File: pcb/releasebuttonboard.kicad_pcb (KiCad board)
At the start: 4 copper layers, 65 x 56 mm, 30 parts, among them SW1 ROTENC, U1 24C16, U2 RASPIPLUSHEADER, U3 OLEDHeader, U4 REncHeader, U5 BtnHeader, U6 PAM8407, U7 REncHeader

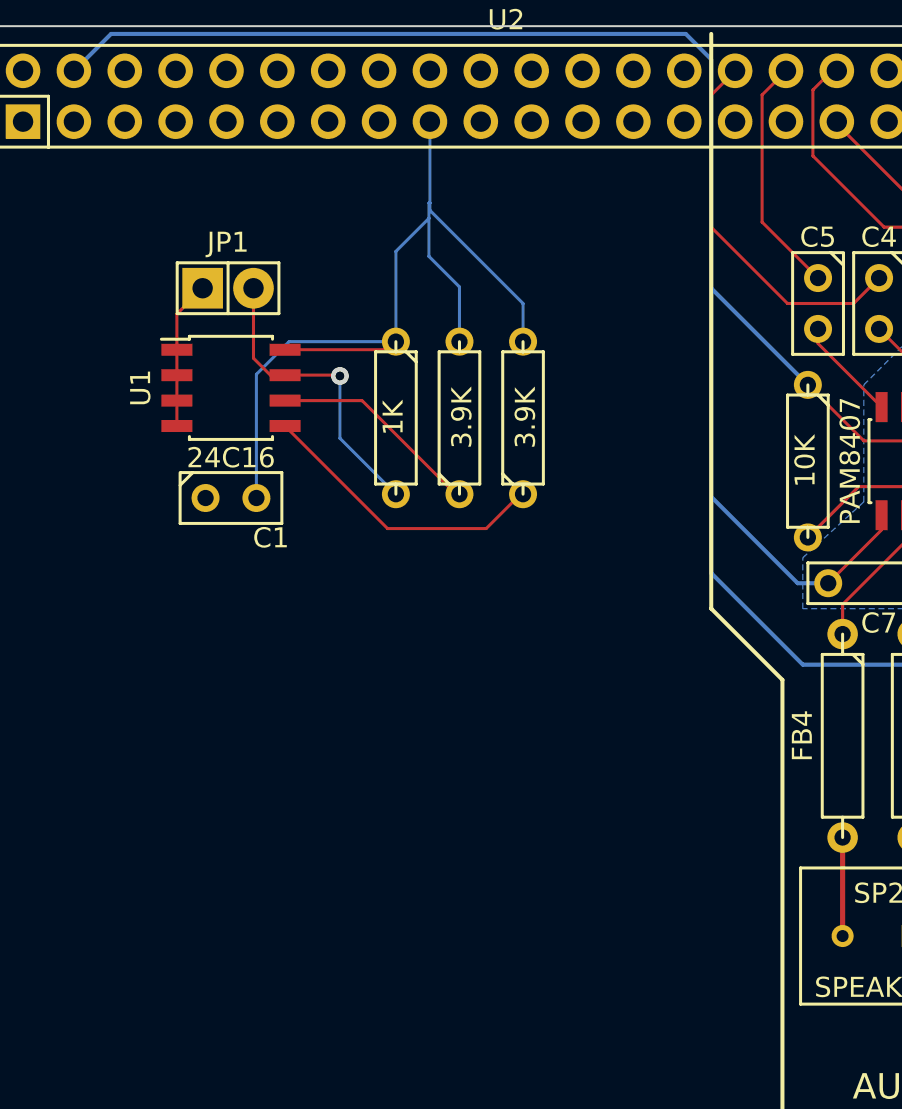
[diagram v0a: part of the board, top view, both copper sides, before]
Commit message: Component placement for ID EEPROM region.
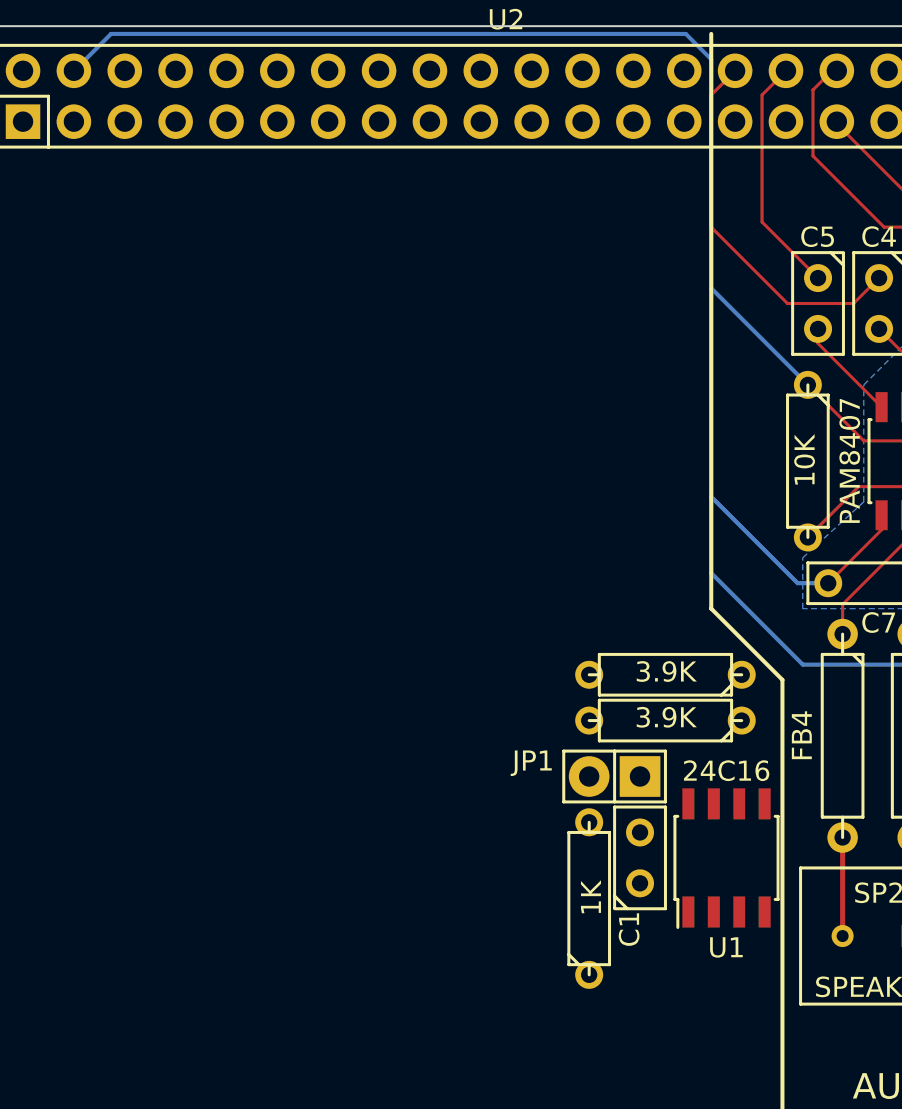
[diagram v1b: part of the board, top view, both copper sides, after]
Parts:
- moved U1 34.1 mm to (139.0, 109.5), turned to 90 degrees
- moved JP1 31.1 mm to (133.4, 105.5), turned to 180 degrees
- moved C1 27.2 mm to (134.7, 109.5), turned to 90 degrees
- moved R1 25.9 mm to (132.1, 111.6), turned to 90 degrees
- moved R3 18.3 mm to (136.0, 102.7), turned to 180 degrees
- moved R2 14.7 mm to (136.0, 100.4), turned to 180 degrees
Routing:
- net VCC: track 69.1 -> 22.3 mm
- net Net-(JP1-Pad2): track 15.2 -> 0.00 mm, vias 1 -> 0
- net /ID_SD: track 14.7 -> 0.00 mm
- net /ID_SC: track 10.8 -> 0.01 mm
- net GND: track 112.9 -> 105.5 mm

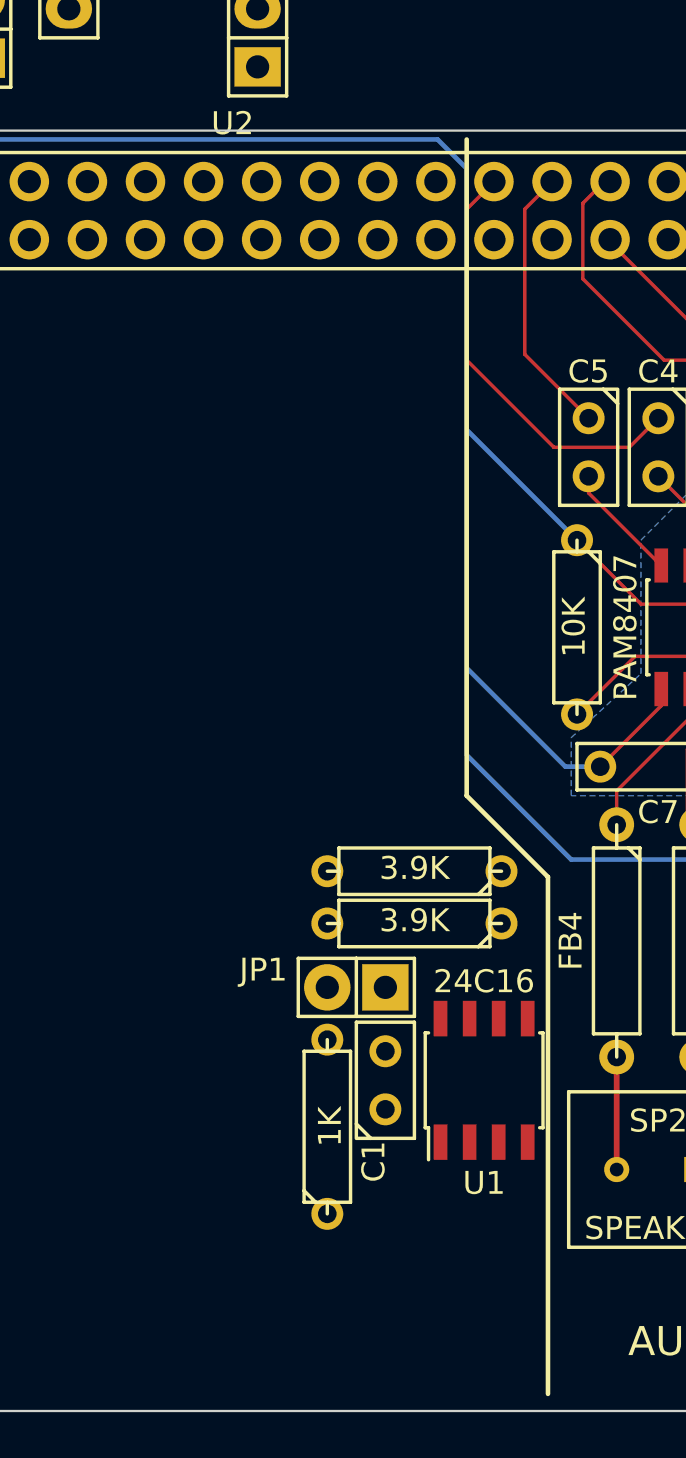
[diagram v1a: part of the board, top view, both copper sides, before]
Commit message: Traces for ID EEPROM circuit portion.
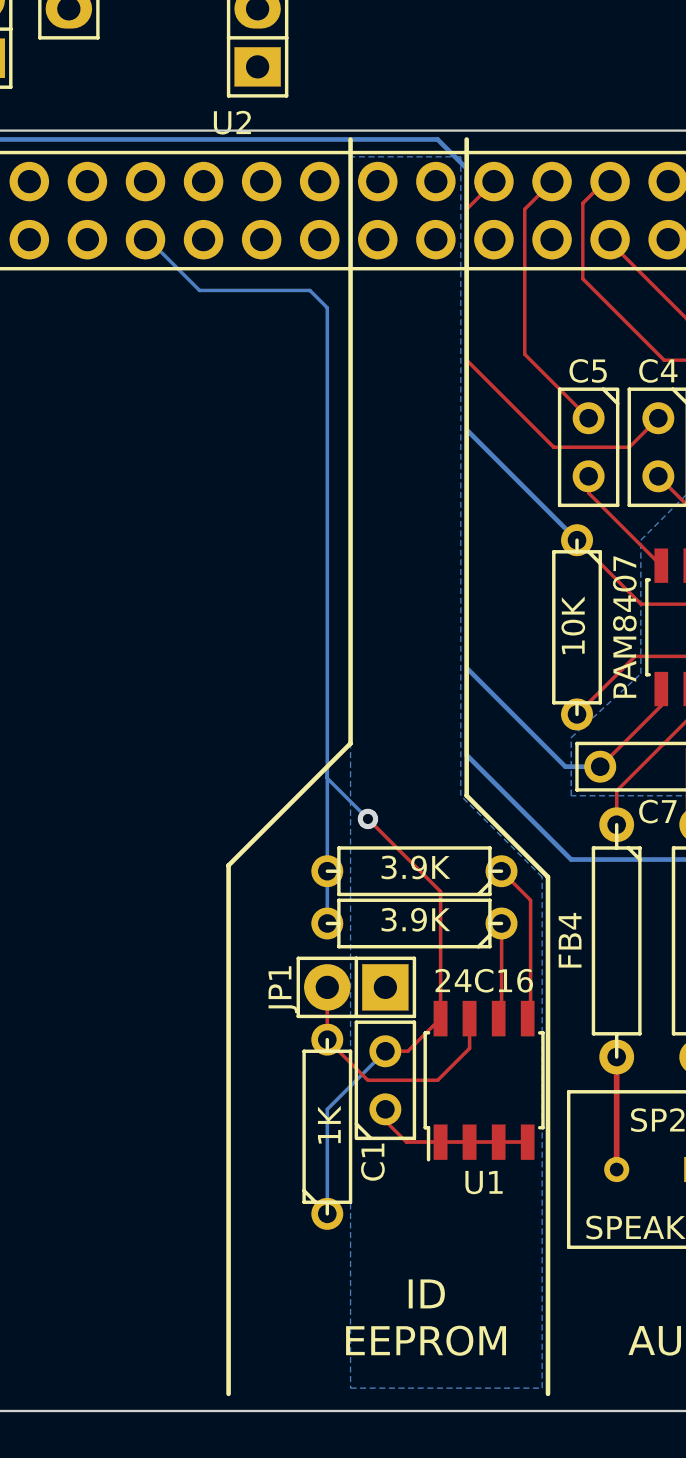
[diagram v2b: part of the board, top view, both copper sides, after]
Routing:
- net VCC: track 22.3 -> 82.6 mm, vias 0 -> 1
- net Net-(JP1-Pad2): track 0.00 -> 11.1 mm
- net GND: track 105.5 -> 112.6 mm
- net /ID_SD: track 0.00 -> 7.02 mm
- net /ID_SC: track 0.01 -> 4.22 mm
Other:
- board text added: "ID EEPROM"
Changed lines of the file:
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@@
   (general
     (links 76)
-    (no_connects 39)
+    (no_connects 24)
     (area 95.449999 67.949999 160.550001 124.050001)
     (thickness 1.6)
-    (drawings 17)
-    (tracks 121)
+    (drawings 21)
+    (tracks 153)
     (zones 0)
     (modules 30)
@@
     (descr "Through hole pin header")
     (tags "pin header")
-    (fp_text reference JP1 (at 4.064 0.762 360) (layer F.SilkS)
-      (effects (font (size 1 1) (thickness 0.15)))
-    )
-    (fp_text value JUMPER (at 5.588 -0.762 360) (layer F.SilkS) hide
+    (fp_text reference JP1 (at 3.302 0 450) (layer F.SilkS)
+      (effects (font (size 1 1) (thickness 0.15)))
+    )
+    (fp_text value JUMPER (at 4.572 -1.778 450) (layer F.SilkS) hide
       (effects (font (size 1 1) (thickness 0.15)))
     )
@@
     (tags R)
     (autoplace_cost180 10)
-    (fp_text reference R1 (at 0 -2 90) (layer F.SilkS) hide
+    (fp_text reference R1 (at -2.286 -1.778 90) (layer F.SilkS) hide
       (effects (font (size 1 1) (thickness 0.15)))
     )
@@
     (pad 1 thru_hole circle (at 0 0) (size 6.2 6.2) (drill 2.75) (layers *.Cu *.Mask F.SilkS))
   )
+  (gr_line (start 133.158 94.804) (end 133.158 68.388) (angle 90) (layer F.SilkS) (width 0.2))
+  (gr_line (start 127.824 100.138) (end 133.158 94.804) (angle 90) (layer F.SilkS) (width 0.2))
+  (gr_line (start 127.824 123.252) (end 127.824 100.138) (angle 90) (layer F.SilkS) (width 0.2))
+  (gr_text "ID\nEEPROM" (at 136.46 119.95) (layer F.SilkS)
+    (effects (font (thickness 0.1905)))
+  )
   (gr_text "This dummy layer is here only to trick DRC into\nconsidering the GND and Supply pins on the\nPi header to be electrically connected.\n\nIt should not be included when manufacturing.\nThis is just a two-layer design.\n" (at 103.694 120.204) (layer In1.Cu)
     (effects (font (size 0.508 0.508) (thickness 0.127)) (justify left))
@@
   (gr_line (start 95.5 71) (end 95.5 121) (angle 90) (layer Edge.Cuts) (width 0.1))
   (gr_arc (start 98.5 71) (end 95.5 71) (angle 90) (layer Edge.Cuts) (width 0.1))
+  (segment (start 139.635 112.236) (end 140.905 112.236) (width 0.1524) (layer F.Cu) (net 1))
+  (segment (start 138.365 112.236) (end 139.635 112.236) (width 0.1524) (layer F.Cu) (net 1))
+  (segment (start 137.095 112.236) (end 138.365 112.236) (width 0.1524) (layer F.Cu) (net 1))
+  (segment (start 134.682 110.806) (end 134.682 111.314) (width 0.1524) (layer F.Cu) (net 1))
+  (segment (start 134.682 111.314) (end 135.604 112.236) (width 0.1524) (layer F.Cu) (net 1))
+  (segment (start 135.604 112.236) (end 137.095 112.236) (width 0.1524) (layer F.Cu) (net 1))
   (segment (start 149.287 87.024) (end 149.287 84.517) (width 0.1524) (layer F.Cu) (net 1))
   (via (at 148.652 83.882) (size 0.889) (layers F.Cu B.Cu) (net 1))
@@
   (segment (start 150.557 92.424) (end 150.557 94.423) (width 0.1524) (layer F.Cu) (net 1))
   (segment (start 150.557 94.423) (end 149.16 95.82) (width 0.1524) (layer F.Cu) (net 1))
+  (segment (start 132.142 95.82) (end 132.142 96.328) (width 0.1524) (layer B.Cu) (net 2))
+  (segment (start 137.095 101.281) (end 137.095 106.836) (width 0.1524) (layer F.Cu) (net 2))
+  (segment (start 133.92 98.106) (end 137.095 101.281) (width 0.1524) (layer F.Cu) (net 2))
+  (via (at 133.92 98.106) (size 0.889) (layers F.Cu B.Cu) (net 2))
+  (segment (start 132.142 96.328) (end 133.92 98.106) (width 0.1524) (layer B.Cu) (net 2))
+  (segment (start 132.142 100.392) (end 132.142 102.678) (width 0.1524) (layer B.Cu) (net 2))
+  (segment (start 124.19 72.77) (end 124.332 72.77) (width 0.1524) (layer B.Cu) (net 2))
+  (segment (start 124.332 72.77) (end 126.554 74.992) (width 0.1524) (layer B.Cu) (net 2))
+  (segment (start 132.142 75.754) (end 132.142 95.82) (width 0.1524) (layer B.Cu) (net 2))
+  (segment (start 132.142 95.82) (end 132.142 100.392) (width 0.1524) (layer B.Cu) (net 2))
+  (segment (start 131.38 74.992) (end 132.142 75.754) (width 0.1524) (layer B.Cu) (net 2))
+  (segment (start 126.554 74.992) (end 131.38 74.992) (width 0.1524) (layer B.Cu) (net 2))
+  (segment (start 132.142 115.378) (end 132.142 110.806) (width 0.1524) (layer B.Cu) (net 2))
+  (segment (start 132.142 110.806) (end 134.682 108.266) (width 0.1524) (layer B.Cu) (net 2))
+  (segment (start 134.682 108.266) (end 135.665 108.266) (width 0.1524) (layer F.Cu) (net 2))
+  (segment (start 135.665 108.266) (end 137.095 106.836) (width 0.1524) (layer F.Cu) (net 2))
   (segment (start 103.87 72.77) (end 104.012 72.77) (width 0.1524) (layer In1.Cu) (net 2))
   (segment (start 104.012 72.77) (end 105.726 74.484) (width 0.1524) (layer In1.Cu) (net 2))
@@
   (segment (start 144.799 98.359) (end 144.879 98.359) (width 0.254) (layer F.Cu) (net 15))
   (segment (start 144.799 113.439) (end 144.799 108.519) (width 0.254) (layer F.Cu) (net 16))
+  (segment (start 132.142 107.758) (end 132.142 105.472) (width 0.1524) (layer F.Cu) (net 17))
+  (segment (start 132.142 107.758) (end 133.92 109.536) (width 0.1524) (layer F.Cu) (net 17))
+  (segment (start 138.365 108.139) (end 138.365 106.836) (width 0.1524) (layer F.Cu) (net 17))
+  (segment (start 136.968 109.536) (end 138.365 108.139) (width 0.1524) (layer F.Cu) (net 17))
+  (segment (start 133.92 109.536) (end 136.968 109.536) (width 0.1524) (layer F.Cu) (net 17))
+  (segment (start 139.762 100.392) (end 141.032 101.662) (width 0.1524) (layer F.Cu) (net 18))
+  (segment (start 141.032 101.662) (end 141.032 106.709) (width 0.1524) (layer F.Cu) (net 18))
+  (segment (start 141.032 106.709) (end 140.905 106.836) (width 0.1524) (layer F.Cu) (net 18))
+  (segment (start 139.762 102.678) (end 139.762 106.709) (width 0.1524) (layer F.Cu) (net 19))
+  (segment (start 139.762 106.709) (end 139.635 106.836) (width 0.1524) (layer F.Cu) (net 19))
   (segment (start 136.89 70.23) (end 136.89 70.244) (width 0.1524) (layer F.Cu) (net 19))
   (segment (start 143.064 93.534) (end 145.604 90.994) (width 0.1524) (layer F.Cu) (net 20))
@@
       )
     )
+  )
+  (zone (net 1) (net_name GND) (layer B.Cu) (hatch edge 0.508)
+    (connect_pads (clearance 0.508))
+    (min_thickness 0.254)
+    (fill yes (arc_segments 16) (thermal_gap 0.508) (thermal_bridge_width 0.508))
+    (polygon
+      (pts
+        (xy 133.158 69.15) (xy 133.158 122.998) (xy 141.54 122.998) (xy 141.54 100.646) (xy 137.984 97.09)
+        (xy 137.984 69.15)
+      )
+    )
